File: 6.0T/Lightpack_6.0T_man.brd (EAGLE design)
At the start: 64.4 x 60.1 mm, 32 parts, among them IC1 AT90USB162, IC2 DM631_SOP24, IC3 DM631_SOP24, J1 DCJ0202, Q1 16Mhz, X1 USB-MICRO-B

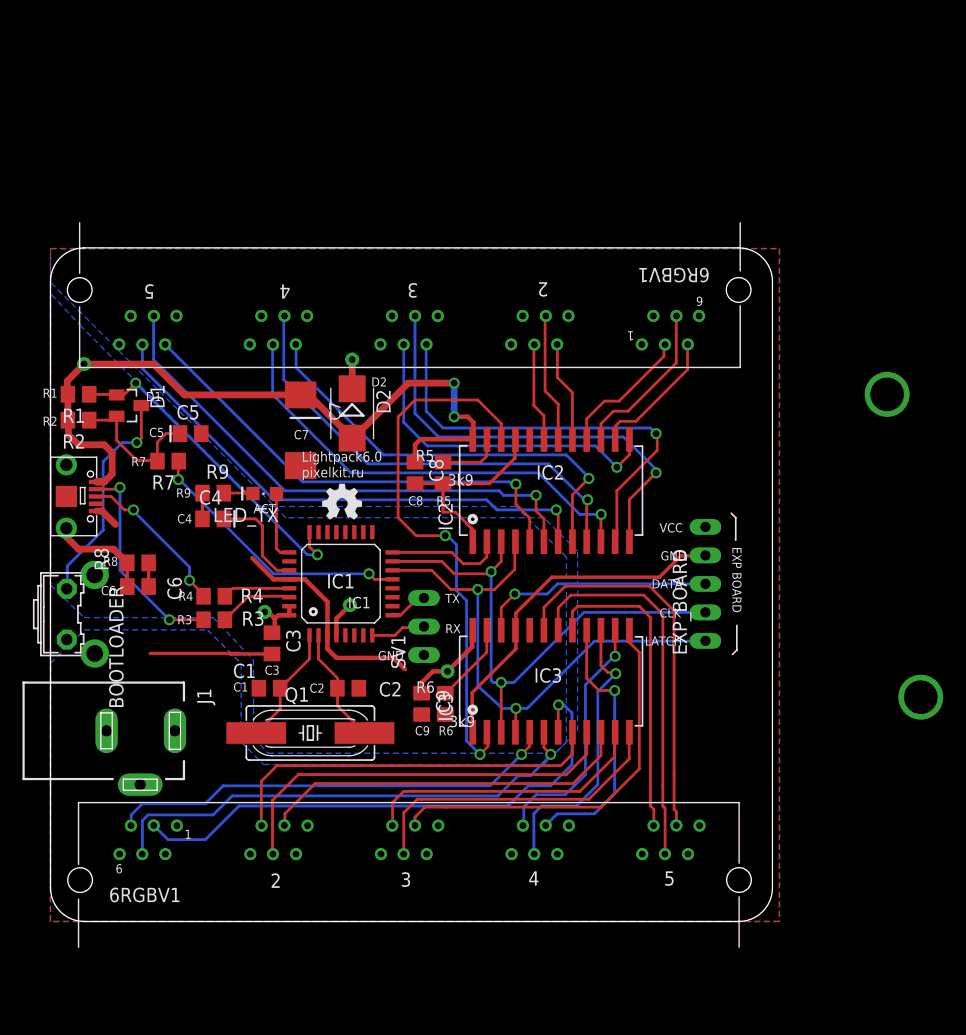
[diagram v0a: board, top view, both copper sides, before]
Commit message: Front-line I/O rearranged
* Button --> DJK02A --> microUSB
* Expand PCB size for Alex case
* Bottom polygons shape changes
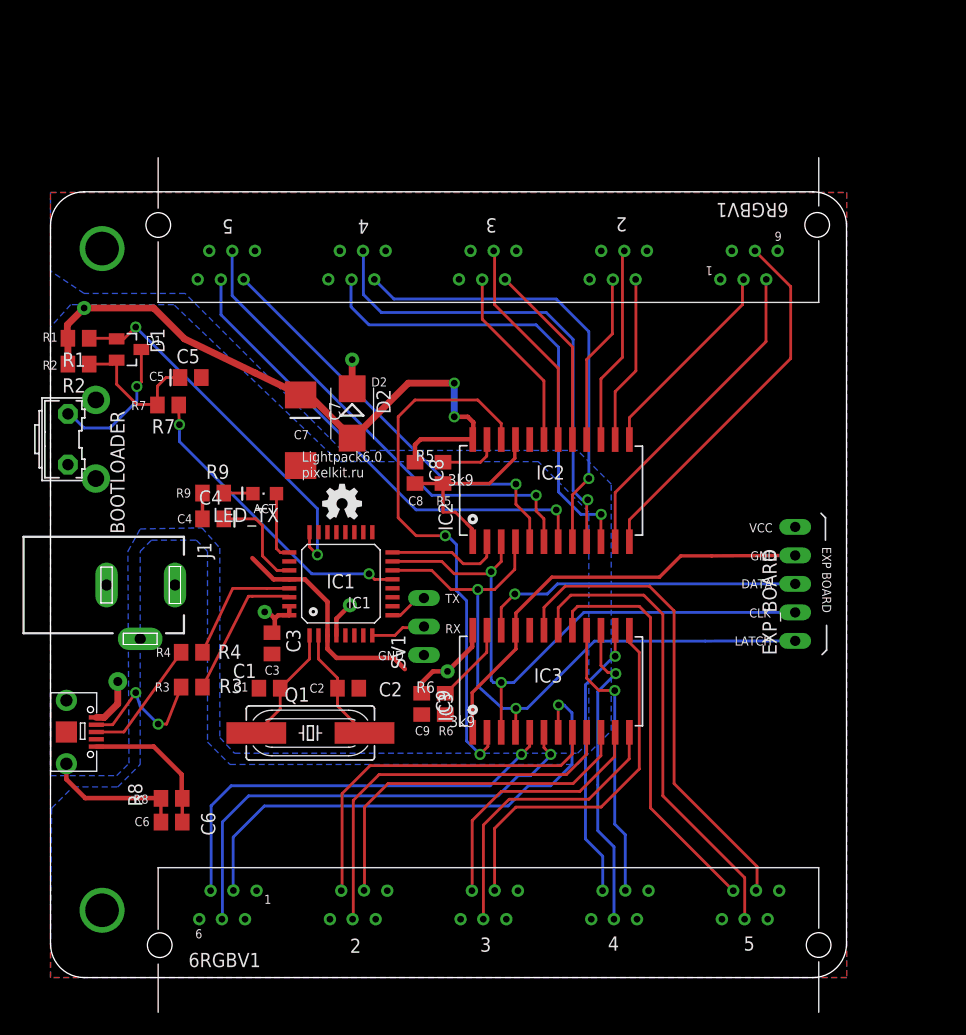
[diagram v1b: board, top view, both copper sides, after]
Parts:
- U$1: value RJ11-5P-REEL-LIGHTPACK6T -> RJ11-5P-REEL-LIGHTPACK6T2
- moved C6 21.2 mm to (11.8, 10.9)
- moved R8 21.2 mm to (11.8, 13.0)
- moved X1 21.0 mm to (5.12, 18.9)
- moved BOOTLOADER 15.6 mm to (3.80, 45.0)
- moved J1 13.0 mm to (9.00, 32.0)
- moved U$2 9.17 mm to (39.1, 2.20)
- moved U$1 9.09 mm to (41.0, 61.8)
- moved EXP_BOARD 8.00 mm to (67.4, 32.1)
- moved R3 6.32 mm to (13.6, 22.9)
- moved R4 5.39 mm to (13.6, 26.0)
- moved C5 5.00 mm to (13.5, 50.5)
- moved D1 5.00 mm to (8.00, 53.0)
- moved R1 5.00 mm to (3.50, 54.0)
- moved R2 5.00 mm to (3.50, 51.7)
- moved R7 5.00 mm to (11.5, 48.1)
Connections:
- net N$12: now also U$1.R1; no longer U$1.R3
- net N$13: now also U$1.G1; no longer U$1.G3
- net N$14: now also U$1.B1; no longer U$1.B3
- net N$15: now also U$1.R2; no longer U$1.R1
- net N$29: now also U$1.G2; no longer U$1.G1
- net N$30: now also U$1.B2; no longer U$1.B1
- net N$38: now also U$1.R3; no longer U$1.R2
- net N$39: now also U$1.G3; no longer U$1.G2
- net N$40: now also U$1.B3; no longer U$1.B2
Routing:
- net N$14: track 30.5 -> 18.5 mm, vias 1 -> 0
- net N$12: track 38.8 -> 29.0 mm, vias 1 -> 0
- net N$43: track 34.5 -> 43.4 mm
- net N$42: track 34.0 -> 42.7 mm
- net N$41: track 27.9 -> 36.6 mm
- net DATA3: track 21.1 -> 29.1 mm
- net CLK: track 49.1 -> 57.1 mm
- net LATCH: track 50.6 -> 58.6 mm
- net N$38: track 9.05 -> 16.8 mm
- net N$40: track 8.86 -> 16.5 mm
- net N$39: track 11.5 -> 19.2 mm
- net N$16: track 19.9 -> 12.4 mm
- net N$13: track 39.7 -> 33.2 mm, vias 1 -> 0
- net D-: track 6.65 -> 12.8 mm
- net N$32: track 18.8 -> 12.8 mm
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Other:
- board size 64.4 x 60.1 mm -> 71 x 70.1 mm

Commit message: 60T improved for casing
* PCB size 76x71mm now
* UART deletted
* ACT LED now on pin 10 instead 25 (need to modify firmware)
* ACT LED thru-hole d3 now (need to test R9)
* 3 mount holes d3 od5
* Significanty alot of space between components
* I/O ports now adjust for Alex case
* Silkscreen info added
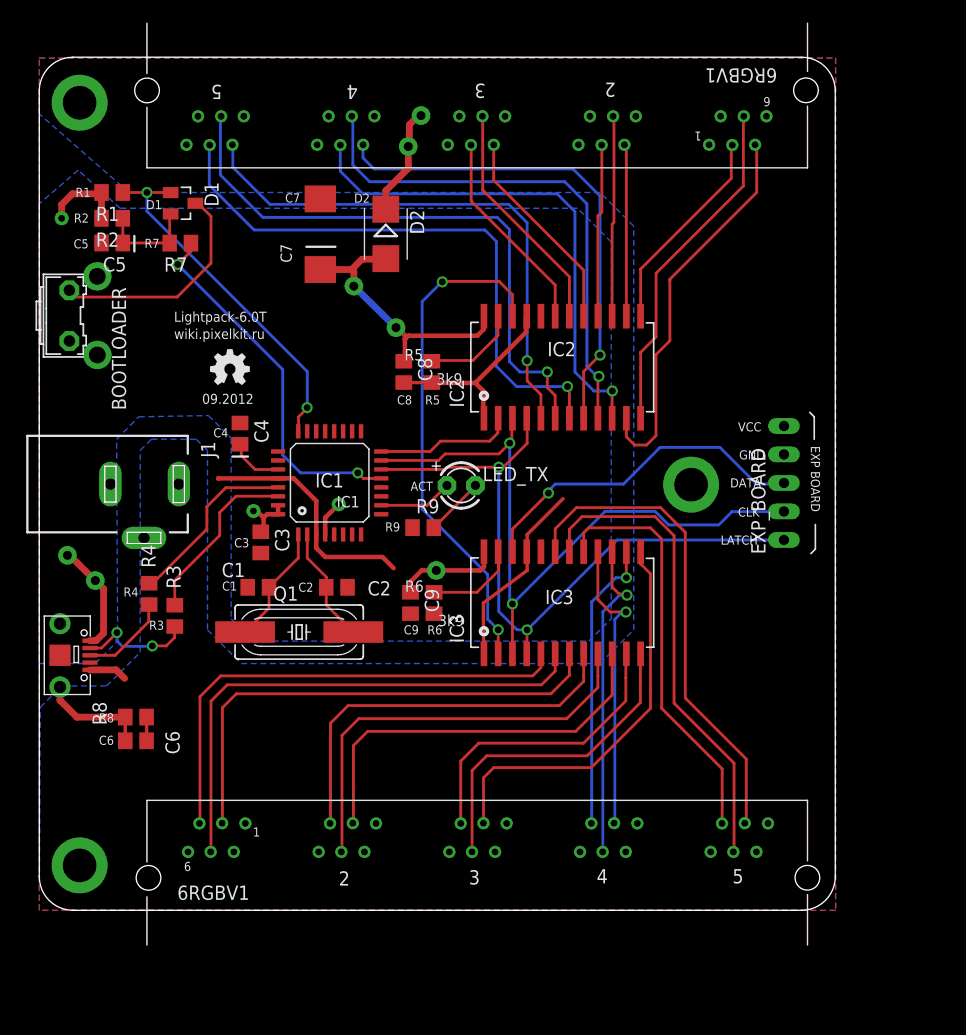
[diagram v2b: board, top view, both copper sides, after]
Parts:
- removed SV1: (no value), _brd-conn:UART3
- LED_TX: device led:CHIPLED_0805 -> adafruit:LED3MM
- moved R9 19.0 mm to (34.2, 37.1)
- moved C7 17.6 mm to (25.1, 63.3), turned to 90 degrees
- moved LED_TX 17.5 mm to (37.6, 40.9), turned to 0 degrees
- moved D2 16.3 mm to (30.9, 63.3)
- moved R7 14.5 mm to (12.6, 62.5)
- moved D1 13.9 mm to (12.8, 66.0)
- moved C5 13.9 mm to (6.50, 62.5), turned to 180 degrees
- moved R1 13.3 mm to (6.50, 67.0)
- moved R2 13.3 mm to (6.50, 64.7)
- moved U$1 12.0 mm to (40.0, 73.8)
- moved IC2 11.0 mm to (46.5, 51.5)
- moved BOOTLOADER 11.0 mm to (3.93, 56.0)
- moved C1 9.06 mm to (19.5, 31.8)
- moved C2 9.06 mm to (26.5, 31.8)
- moved C8 9.06 mm to (32.5, 51.0)
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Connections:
- removed net N$4: IC1.9, SV1.3-R
- removed net N$8: IC1.25, LED_TX.A
- net GND: no longer SV1.1-L
- net N$3: now also IC1.10, LED_TX.A; no longer IC1.8, SV1.2
- net N$37: now also LED_TX.K; no longer LED_TX.C
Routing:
- net GND: track 93.4 -> 62.1 mm
- net +5V: track 79.5 -> 60.0 mm, vias 7 -> 8
- net N$5: track 37.6 -> 48.3 mm
- net N$6: track 42.9 -> 53.0 mm
- net N$7: track 43.1 -> 52.4 mm
- net N$16: track 12.4 -> 20.2 mm, vias 1 -> 0
- net N$57: track 2.60 -> 9.90 mm, vias 1 -> 2
- net N$8: track 6.19 -> 0.00 mm
- net N$12: track 29.0 -> 34.7 mm
- net CLK: track 57.1 -> 62.7 mm
- net HWB: track 27.4 -> 32.9 mm
- net D+: track 11.4 -> 16.3 mm
- net N$47: track 13.7 -> 9.03 mm
- net N$18: track 39.4 -> 44.0 mm, vias 1 -> 0
- net N$17: track 9.34 -> 4.86 mm
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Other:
- board size 71 x 70.1 mm -> 71 x 76.1 mm
- board text added: "09.2012"
- board text added: "Lightpack-6.0T"
- board text added: "wiki.pixelkit.ru"
- board text removed: "Lightpack6.0"
- board text removed: "RX"
- board text removed: "TX"
- board text removed: "pixelkit.ru"
